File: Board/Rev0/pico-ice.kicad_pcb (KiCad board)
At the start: 4 copper layers, 22.9 x 61 mm, 106 parts, among them J1 USB_C_Receptacle_USB2.0, J10 2x3_2.54mm_Female, J11 2x3_2.54mm_Female, J3 6X2 Female Header, J4 6X2 Female Header, J5 Conn_ARM_JTAG_SWD_10, J6 6X2 Female Header, J7 6X2 Female Header, J8 6X2 Female Header, J9 BOOT_SEL, SW1 PTS820 J25K SMTR LFS, SW2 PTS820 J25K SMTR LFS, U1 NCP1117ST33T3G, U2 W25Q32JVSSIQ, U3 RP2040, U4 CL9293A12L5M, U5 APS6404L-3SQN-SN, U6 ICE40UP5K-SG48ITR, U8 W25Q32JVSSIQ, Y1 12 MHz

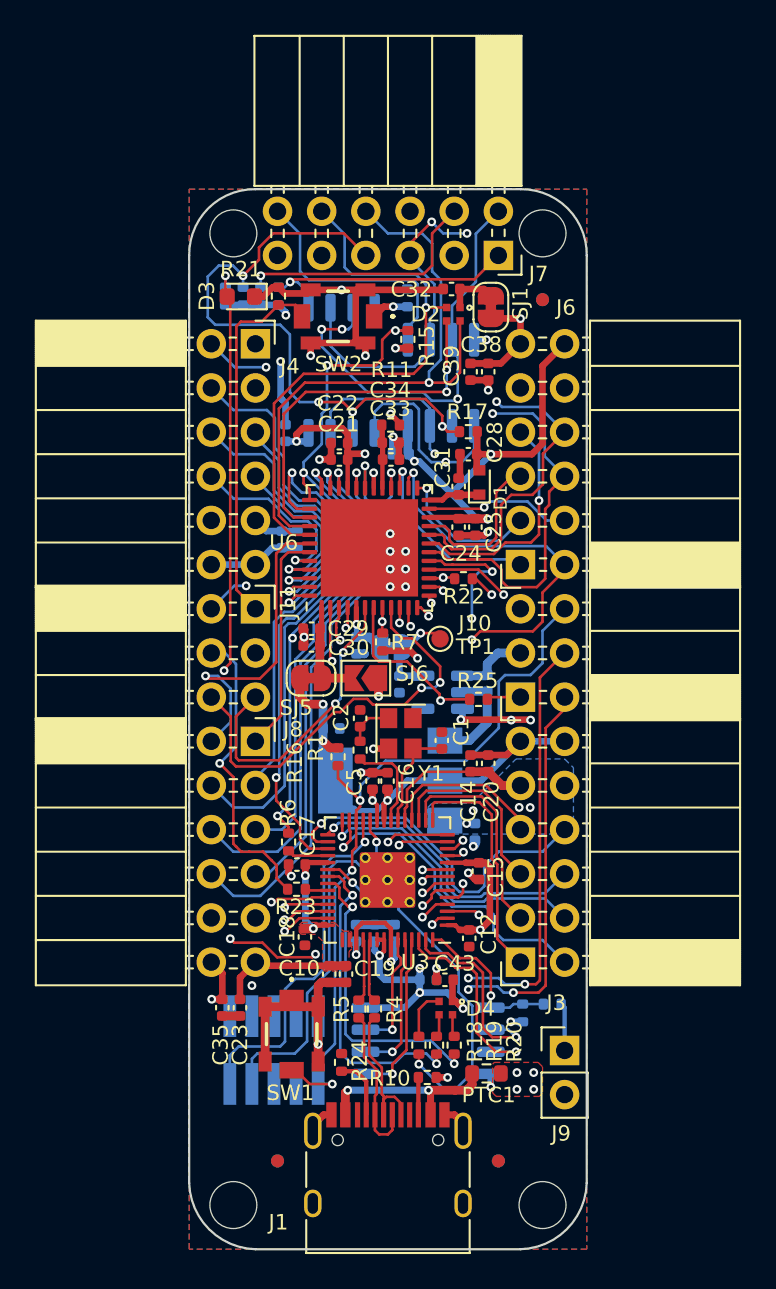
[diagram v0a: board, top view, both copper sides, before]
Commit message: Cleaned up silkscreen
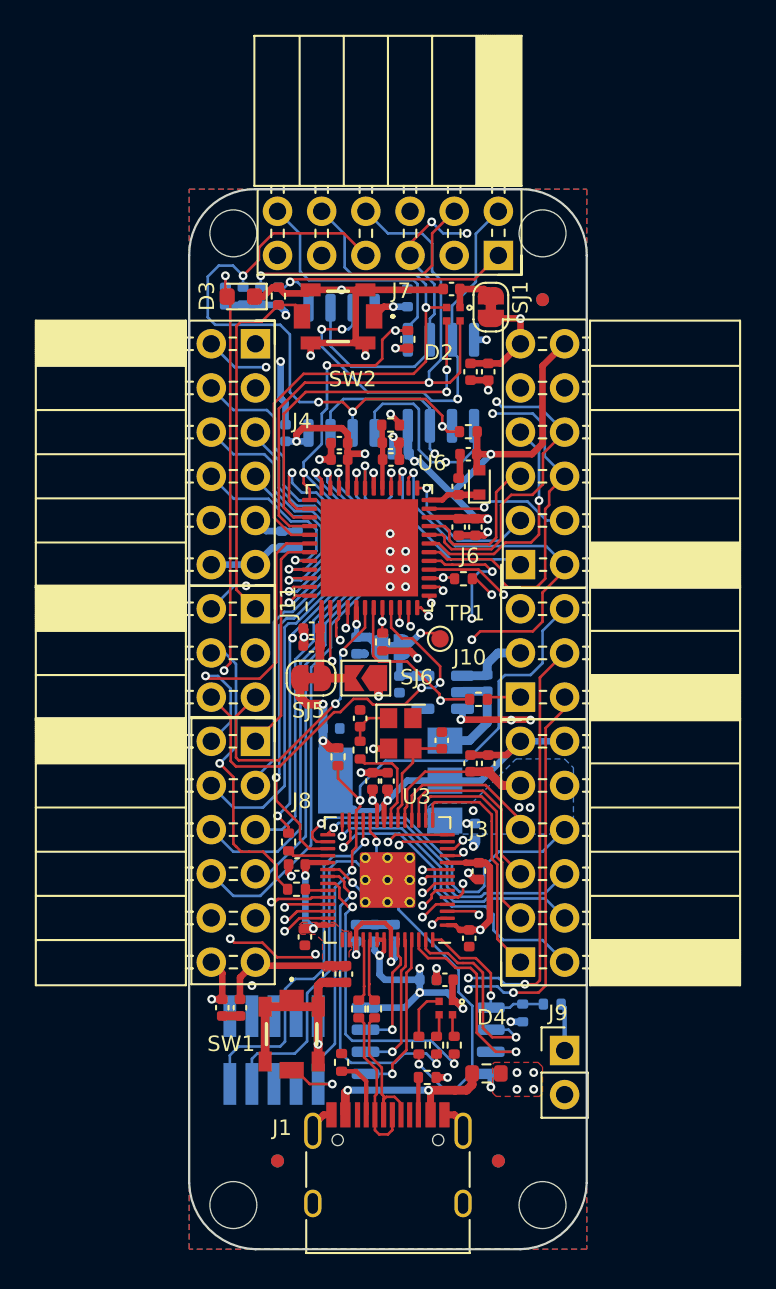
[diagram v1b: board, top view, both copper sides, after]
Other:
- board text removed: "A"

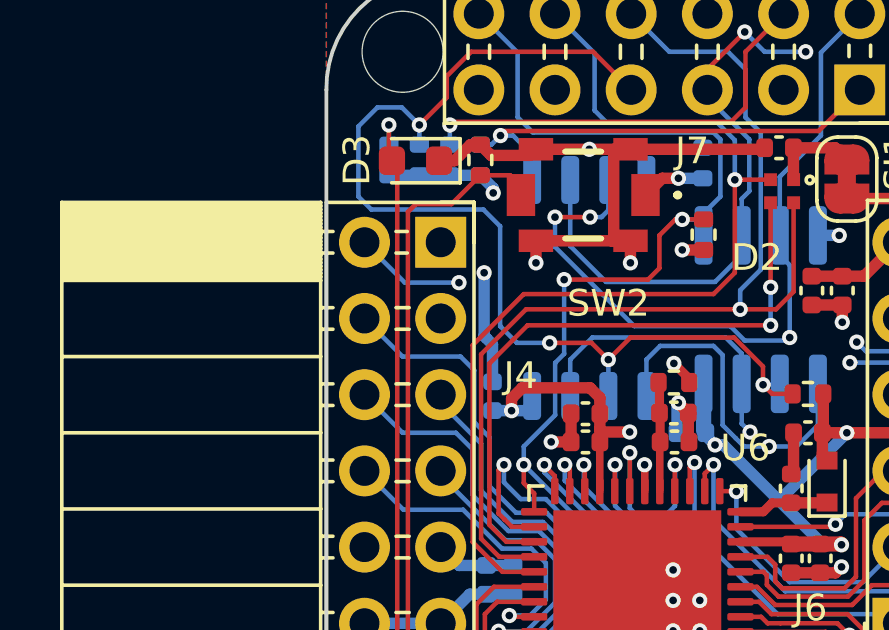
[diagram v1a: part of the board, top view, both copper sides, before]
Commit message: Added a few pin numbers on the silkscreen
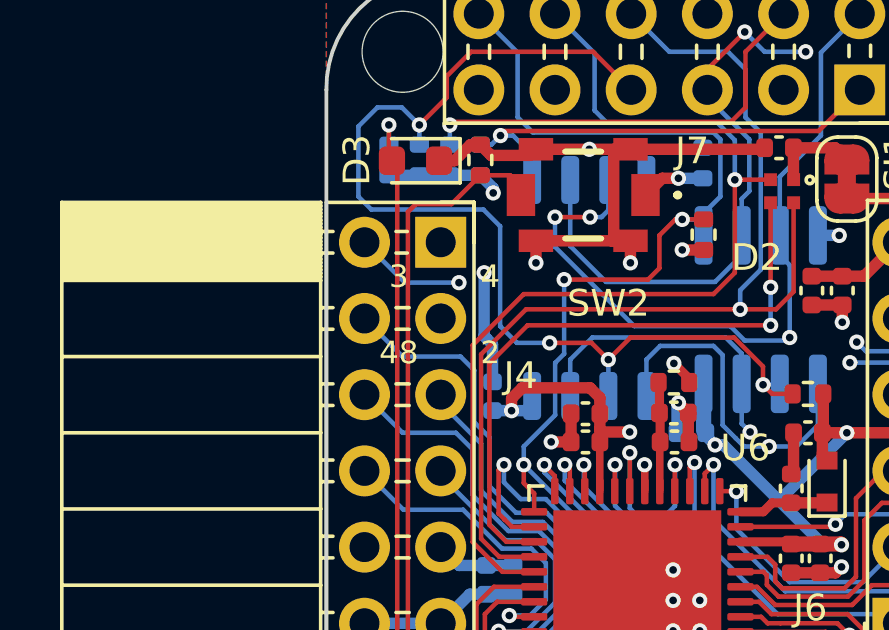
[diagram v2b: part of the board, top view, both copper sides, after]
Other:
- board text added: "2"
- board text added: "3"
- board text added: "4"
- board text added: "48"
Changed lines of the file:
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@@
   (gr_arc (start 80.01 73.66) (mid 82.720683 74.759317) (end 83.82 77.47) (layer "Edge.Cuts") (width 0.127))
   (gr_arc (start 83.82 130.81) (mid 82.673092 133.473092) (end 80.01 134.62) (layer "Edge.Cuts") (width 0.127))
+  (gr_text "4" (at 66.167 83.82) (layer "B.SilkS")
+    (effects (font (size 0.75 0.75) (thickness 0.12)) (justify mirror))
+  )
+  (gr_text "3" (at 63.373 83.82) (layer "B.SilkS")
+    (effects (font (size 0.75 0.75) (thickness 0.12)) (justify mirror))
+  )
+  (gr_text "48" (at 63.373 86.233) (layer "F.SilkS")
+    (effects (font (size 0.75 0.75) (thickness 0.1)))
+  )
+  (gr_text "2" (at 66.421 86.233) (layer "F.SilkS")
+    (effects (font (size 0.75 0.75) (thickness 0.1)))
+  )
+  (gr_text "4" (at 66.421 83.693) (layer "F.SilkS")
+    (effects (font (size 0.75 0.75) (thickness 0.1)))
+  )
+  (gr_text "3" (at 63.373 83.693) (layer "F.SilkS")
+    (effects (font (size 0.75 0.75) (thickness 0.1)))
+  )
   (segment (start 71.0948 83.2356) (end 71.0946 83.2358) (width 0.381) (layer "F.Cu") (net 1))
   (segment (start 78.156 85.2168) (end 78.1558 85.217) (width 0.381) (layer "F.Cu") (net 1))

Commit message: Updated the silkscreen layer
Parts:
- added LOGO1: tinyVS Logo, CUSTOM:tinyAI_logo, F.Cu at (64.5, 126.7)
- added LOGO2: WEEE Logo, CUSTOM:WEEE logo, B.Cu at (75.6, 115.2)
- added LOGO3: Pb free Logo, CUSTOM:Pb free logo, B.Cu at (71.8, 93.7)
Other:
- board text added: "+"
- board text added: "-"
- board text added: "10"
- board text added: "11"
- board text added: "18"
- board text added: "19"
- board text added: "20"
- board text added: "21"
- board text added: "23"
- board text added: "25"
- board text added: "26"
- board text added: "27"
- board text added: "28"
- board text added: "31"
- board text added: "32"
- board text added: "34"
- board text added: "35"
- board text added: "36"
- board text added: "38"
- board text added: "42"
- board text added: "43"
- board text added: "44"
- board text added: "45"
- board text added: "46"
- board text added: "47"
- board text added: "6"
- board text added: "9"
- board text added: "A1"
- board text added: "A2"
- board text added: "A3"
- board text added: "A4"
- board text added: "B1"
- board text added: "B2"
- board text added: "B3"
- board text added: "B4"
- board text added: "GND"
- board text added: "PICO-ICE V1"
- board text added: "RS"
- board text added: "VBUS"
- board text added: "~0"
- board text added: "~2"
- board text added: "~3"

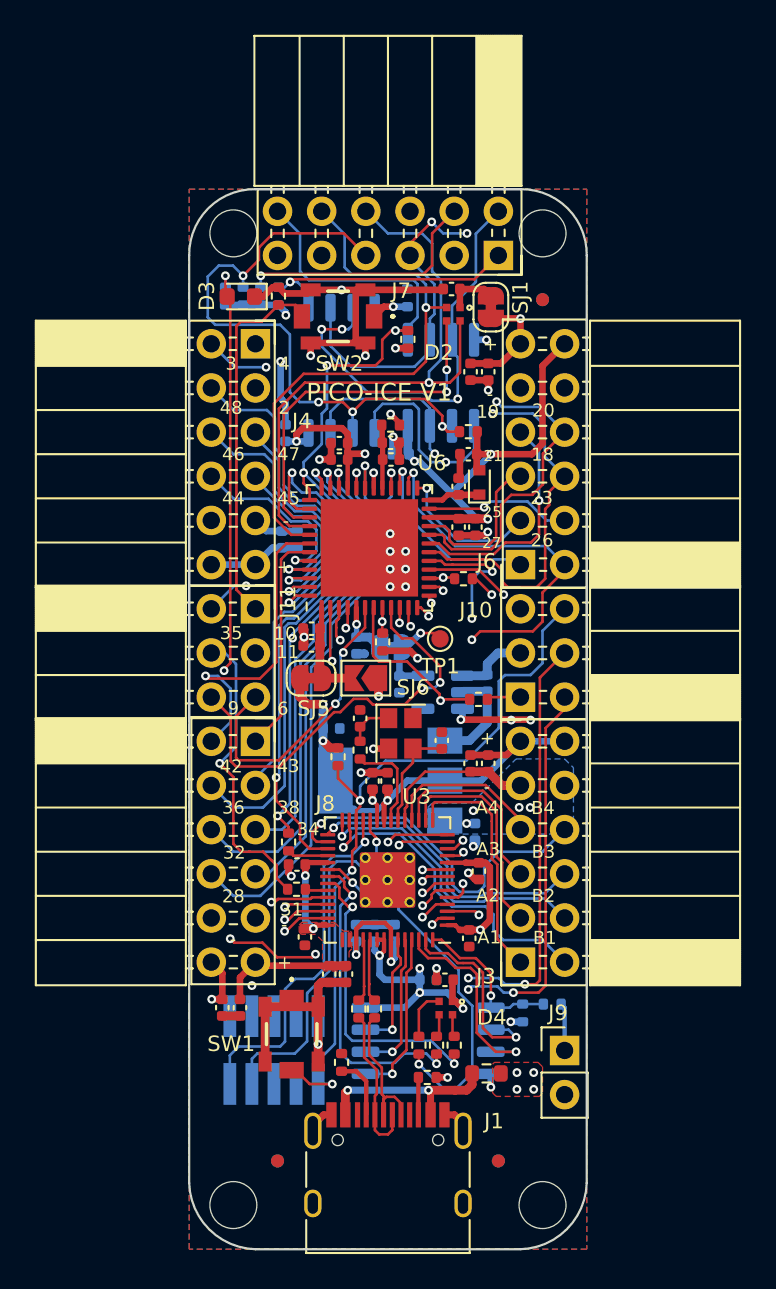
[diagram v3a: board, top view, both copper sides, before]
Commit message: Silkscreen changes
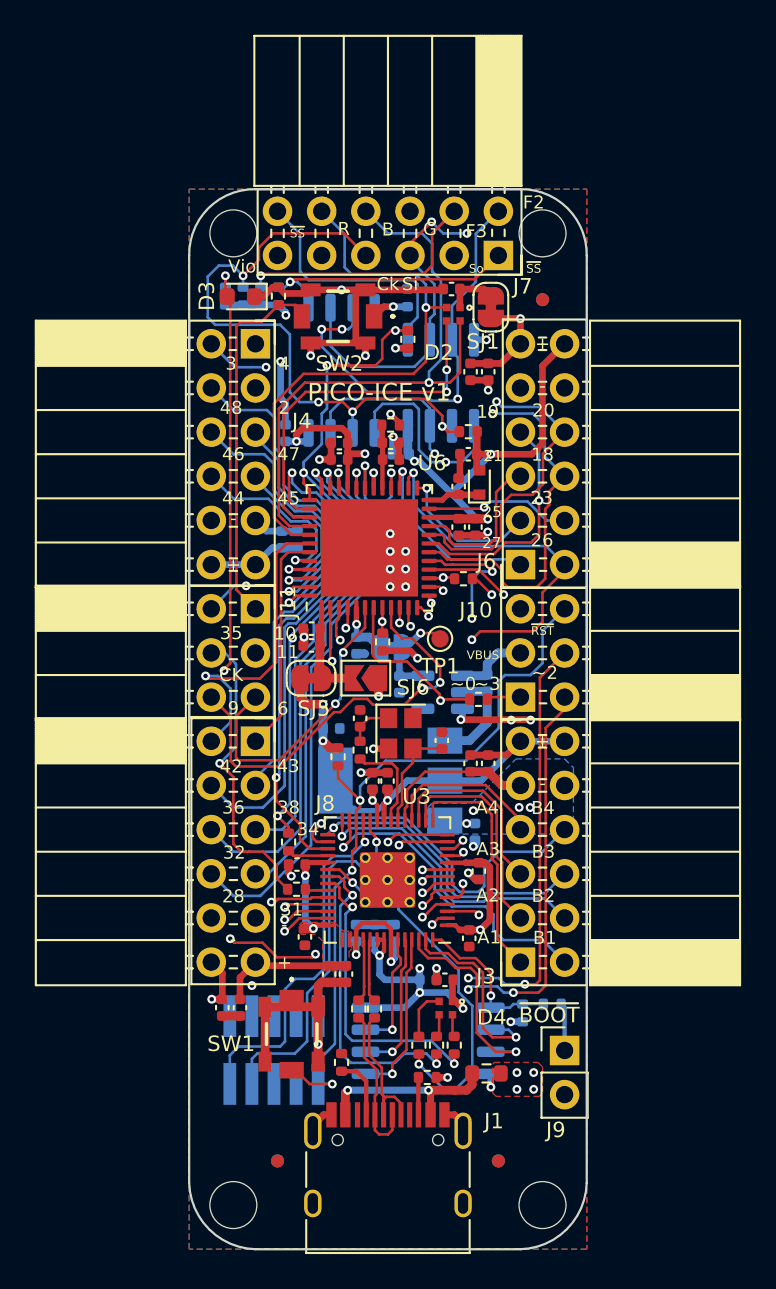
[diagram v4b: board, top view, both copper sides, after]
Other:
- board text added: "B"
- board text added: "CK"
- board text added: "Ck"
- board text added: "F2"
- board text added: "F3"
- board text added: "G"
- board text added: "PICO-ICE v1"
- board text added: "R"
- board text added: "Si"
- board text added: "So"
- board text added: "Vio"
- board text added: "~{BOOT}"
- board text added: "~{RST}"
- board text added: "~{SS}"
- board text removed: "PICO-ICE V1"

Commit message: Updated the logo
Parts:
- moved LOGO1 0.81 mm to (64.5, 125.9)

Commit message: Updated SCH/PCB
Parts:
- removed J5: Conn_ARM_JTAG_SWD_10, Connector_PinHeader_1.27mm:PinHeader_2x05_P1.27mm_Vertical_SMD
- added J2: SWD, Connector_PinHeader_2.54mm:PinHeader_1x02_P2.54mm_Vertical, F.Cu at (62.2, 120.7)
- moved C35 4.64 mm to (67.1, 118.8)
- moved C23 4.59 mm to (68.0, 118.8)
- moved J9 3.59 mm to (80.0, 120.7), turned to 90 degrees
- moved R2 3.49 mm to (78.4, 120.2), turned to 90 degrees
- moved R18 3.23 mm to (74.2, 119.7), turned to -90 degrees
- moved R3 2.81 mm to (77.4, 120.2), turned to -90 degrees
- moved C8 2.64 mm to (72.1, 119.2)
- moved U2 2.64 mm to (72.1, 122.7)
- moved SW1 1.65 mm to (68.4, 122.8)
- moved R19 1.59 mm to (74.2, 121.6)
- moved R4 1.48 mm to (72.0, 119.4)
- moved R5 1.48 mm to (71.1, 119.4)
- moved R24 1.44 mm to (71.1, 124.1)
- moved LOGO1 0.57 mm to (64.7, 125.4)
- moved R20 0.50 mm to (75.8, 122.6), turned to 0 degrees
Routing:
- net GND: track 79.8 -> 39.4 mm, vias 27 -> 29
- net /PICO_LED_R: track 21.2 -> 10.2 mm
- net +3V3: track 130.5 -> 121.8 mm, vias 22 -> 19
- net /SWD: track 21.0 -> 15.2 mm
- net /ICE_DONE_ADC0: track 41.1 -> 46.4 mm
- net /ADC3: track 38.8 -> 42.2 mm, vias 3 -> 2
- net /ADC2: track 41.0 -> 44.3 mm, vias 3 -> 2
- net /PICO_LED_G: track 18.2 -> 15.0 mm
- net /QSPI_SD3: track 6.98 -> 9.56 mm
- net /QSPI_SCLK: track 8.32 -> 10.7 mm
- net /QSPI_SD0: track 9.72 -> 12.1 mm
- net Net-(D4-Pad4): track 2.90 -> 0.91 mm
- net /QSPI_SD2: track 12.0 -> 10.1 mm
- net /ICE_FLASH_IO3: track 51.4 -> 52.7 mm
- net /PICO_LED_B: track 17.3 -> 16.0 mm
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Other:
- board text added: "SWCK"
- board text added: "SWD"
